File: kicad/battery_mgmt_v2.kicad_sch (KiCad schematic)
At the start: 16 parts, among them J601 BATTERY_CONN, SW401 SW_Push, U402 BQ21061

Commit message: refactor, fix issues, ready for first design
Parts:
- added TP301: VIO_TEST, symbol Connector:TestPoint
- C407: value 1uF -> 2.2uF
- TP602: value VB_TEST -> BATTP_TEST
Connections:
- net CHRG: no longer R403.1, R404.1, R405.1, R406.1
- net VIO: now reaches C404.1, U402.13 (VDD), U402.17 (VIO)
- net VIO: now also R403.1, R404.1, R405.1, R406.1, TP301.1
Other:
- note added: "Try and keep LDO connections <100-150 mA"
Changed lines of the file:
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@@
+	)
+	(junction
+		(at 170.18 83.82)
+		(diameter 0)
+		(color 0 0 0 0)
 	)
 	(junction
@@
 	)
 	(junction
-		(at 170.18 83.82)
-		(diameter 0)
-		(color 0 0 0 0)
-	)
-	(junction
 		(at 189.23 76.2)
 		(diameter 0)
@@
 		(color 0 0 0 0)
 	)
+	(junction
+		(at 170.18 86.36)
+		(diameter 0)
+		(color 0 0 0 0)
+	)
 	(wire
 		(pts
@@
 	(wire
 		(pts
+			(xy 167.64 121.92) (xy 167.64 127)
+		)
+		(stroke
+			(width 0)
+			(type default)
+		)
+	)
+	(wire
+		(pts
 			(xy 177.8 63.5) (xy 170.18 63.5)
 		)
@@
 	(wire
 		(pts
+			(xy 147.32 121.92) (xy 147.32 127)
+		)
+		(stroke
+			(width 0)
+			(type default)
+		)
+	)
+	(wire
+		(pts
 			(xy 130.81 88.9) (xy 139.7 88.9)
 		)
@@
 	(wire
 		(pts
+			(xy 176.53 121.92) (xy 176.53 127)
+		)
+		(stroke
+			(width 0)
+			(type default)
+		)
+	)
+	(wire
+		(pts
 			(xy 147.32 135.89) (xy 147.32 134.62)
 		)
@@
 	(wire
 		(pts
+			(xy 170.18 86.36) (xy 173.99 86.36)
+		)
+		(stroke
+			(width 0)
+			(type default)
+		)
+	)
+	(wire
+		(pts
 			(xy 137.16 135.89) (xy 137.16 134.62)
 		)
@@
 	(wire
 		(pts
+			(xy 97.79 133.35) (xy 97.79 137.16)
+		)
+		(stroke
+			(width 0)
+			(type default)
+		)
+	)
+	(wire
+		(pts
 			(xy 189.23 76.2) (xy 196.85 76.2)
 		)
@@
 			(width 0)
 			(type default)
+		)
+	)
+	(wire
+		(pts
+			(xy 137.16 121.92) (xy 137.16 127)
+		)
+		(stroke
+			(width 0)
+			(type default)
+		)
+	)
+	(text "Try and keep LDO\nconnections <100-150 mA"
+		(exclude_from_sim no)
+		(at 208.026 89.916 0)
+		(effects
+			(font
+				(size 1.27 1.27)
+			)
+		)
+	)
+	(label "VIO"
+		(at 97.79 133.35 270)
+		(fields_autoplaced yes)
+		(effects
+			(font
+				(size 1.27 1.27)
+			)
+			(justify right bottom)
+		)
+	)
+	(label "VIO"
+		(at 173.99 86.36 180)
+		(fields_autoplaced yes)
+		(effects
+			(font
+				(size 1.27 1.27)
+			)
+			(justify right bottom)
+		)
+	)
+	(label "VIO"
+		(at 147.32 121.92 270)
+		(fields_autoplaced yes)
+		(effects
+			(font
+				(size 1.27 1.27)
+			)
+			(justify right bottom)
+		)
+	)
+	(label "VIO"
+		(at 167.64 121.92 270)
+		(fields_autoplaced yes)
+		(effects
+			(font
+				(size 1.27 1.27)
+			)
+			(justify right bottom)
+		)
+	)
+	(label "VIO"
+		(at 176.53 121.92 270)
+		(fields_autoplaced yes)
+		(effects
+			(font
+				(size 1.27 1.27)
+			)
+			(justify right bottom)
+		)
+	)
+	(label "VIO"
+		(at 137.16 121.92 270)
+		(fields_autoplaced yes)
+		(effects
+			(font
+				(size 1.27 1.27)
+			)
+			(justify right bottom)
 		)
 	)
@@
 		)
 	)
-	(hierarchical_label "CHRG"
-		(shape input)
-		(at 167.64 127 90)
-		(fields_autoplaced yes)
-		(effects
-			(font
-				(size 1.27 1.27)
-			)
-			(justify left)
-		)
-	)
 	(hierarchical_label "PG_N"
 		(shape output)
@@
 		)
 	)
-	(hierarchical_label "CHRG"
-		(shape input)
-		(at 147.32 127 90)
-		(fields_autoplaced yes)
-		(effects
-			(font
-				(size 1.27 1.27)
-			)
-			(justify left)
-		)
-	)
 	(hierarchical_label "SCL"
 		(shape input)
@@
 		)
 	)
-	(hierarchical_label "CHRG"
-		(shape input)
-		(at 176.53 127 90)
-		(fields_autoplaced yes)
-		(effects
-			(font
-				(size 1.27 1.27)
-			)
-			(justify left)
-		)
-	)
 	(hierarchical_label "PG_N"
 		(shape output)
@@
 		)
 	)
-	(hierarchical_label "CHRG"
-		(shape input)
-		(at 137.16 127 90)
-		(fields_autoplaced yes)
-		(effects
-			(font
-				(size 1.27 1.27)
-			)
-			(justify left)
-		)
-	)
 	(hierarchical_label "SCL"
 		(shape input)
@@
 			)
 		)
-		(property "Value" "VB_TEST"
+		(property "Value" "BATTP_TEST"
 			(at 103.378 129.54 90)
 			(effects
@@
 			)
 		)
-		(property "Value" "1uF"
+		(property "Value" "2.2uF"
 			(at 199.898 82.296 0)
 			(effects
@@
 					(unit 1)
 				)
+			)
+		)
+	)
+	(symbol
+		(lib_id "Connector:TestPoint")
+		(at 97.79 137.16 270)
+		(unit 1)
+		(exclude_from_sim no)
+		(in_bom yes)
+		(on_board yes)
+		(dnp no)
+		(property "Reference" "TP301"
+			(at 89.154 138.176 90)
+			(effects
+				(font
+					(size 1.27 1.27)
+				)
+				(justify left)
+			)
+		)
+		(property "Value" "VIO_TEST"
+			(at 103.378 138.43 90)
+			(effects
+				(font
+					(size 1.27 1.27)
+				)
+				(justify left)
+			)
+		)
+		(property "Footprint" ""
+			(at 97.79 142.24 0)
+			(effects
+				(font
+					(size 1.27 1.27)
+				)
+				(hide yes)
+			)
+		)
+		(property "Datasheet" "~"
+			(at 97.79 142.24 0)
+			(effects
+				(font
+					(size 1.27 1.27)
+				)
+				(hide yes)
+			)
+		)
+		(property "Description" "test point"
+			(at 97.79 137.16 0)
+			(effects
+				(font
+					(size 1.27 1.27)
+				)
+				(hide yes)
+			)
+		)
+		(pin "1"
+		)
+		(instances
+			(project "kicad"
+				(path "/97e37379-fec6-4f0d-82d9-4ea53516bb02/d2226d13-9ee7-410c-817d-a66f223af34c"
+					(reference "TP301")
+					(unit 1)
+				)

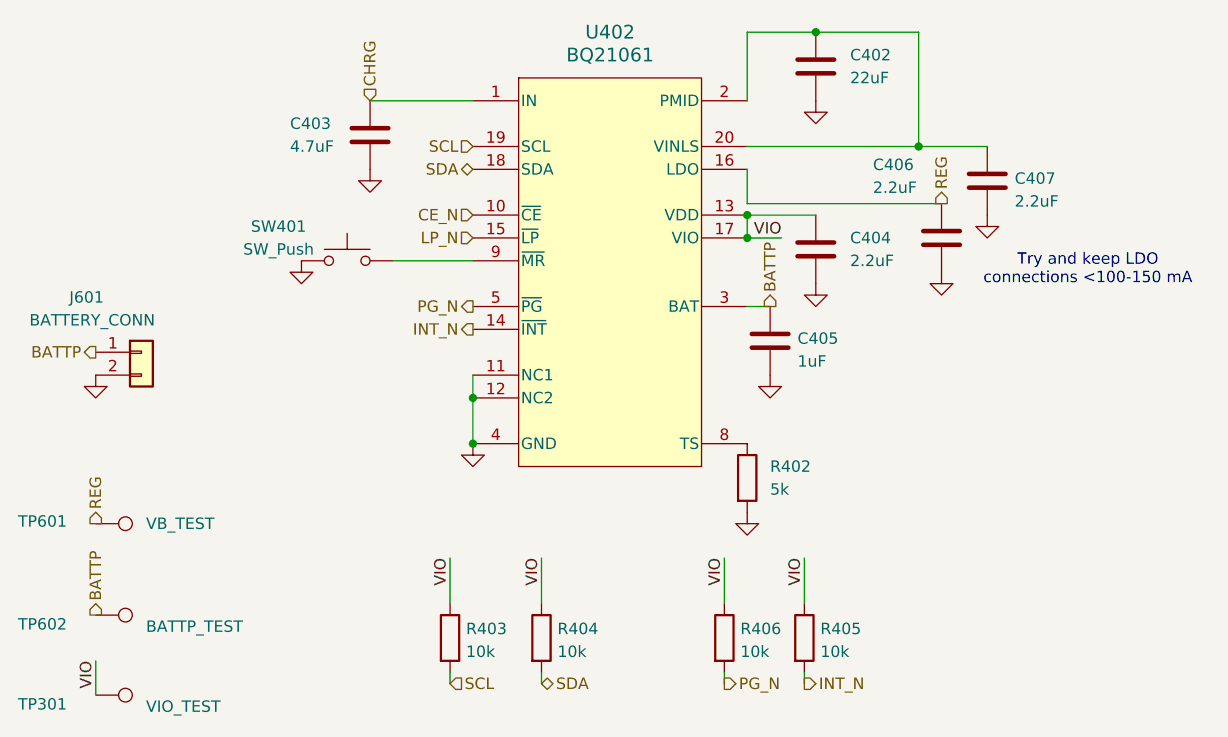
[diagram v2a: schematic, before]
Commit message: essentially finish schematic, start adding footprints, add new footprints
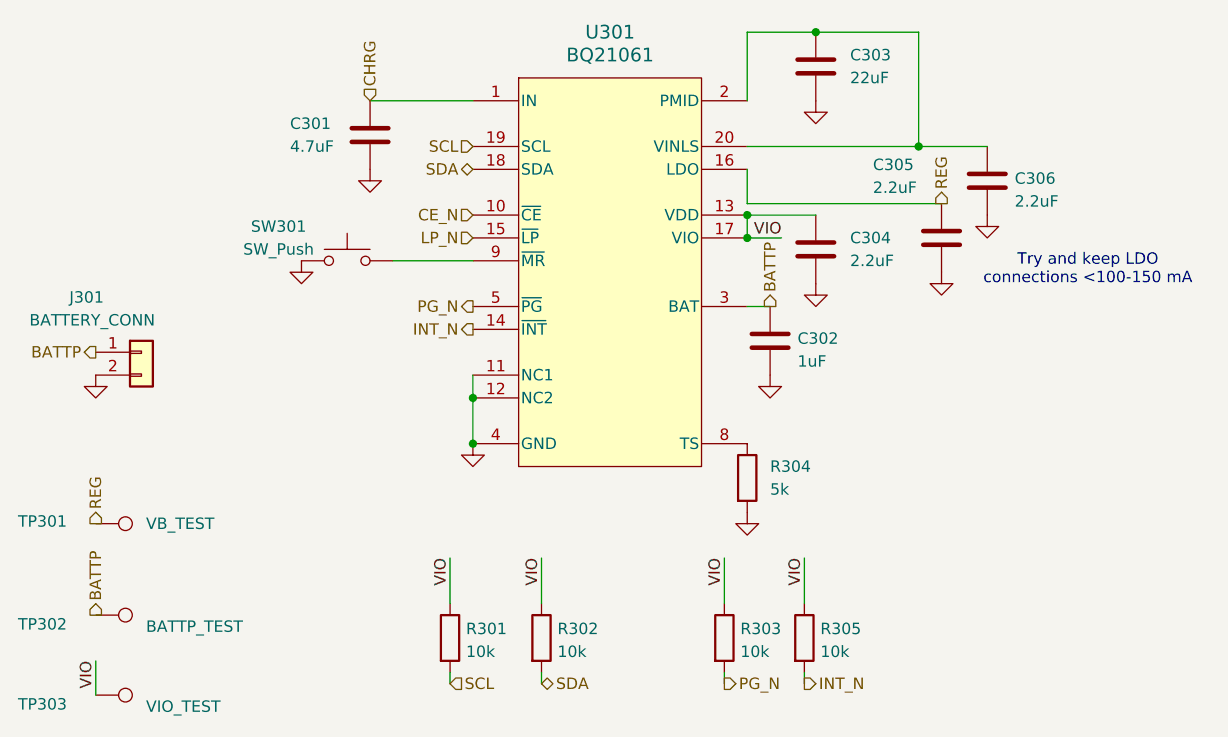
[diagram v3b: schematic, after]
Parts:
- C301: renamed from C403; footprint (none) -> Capacitor_SMD:C_0805_2012Metric_Pad1.18x1.45mm_HandSolder
- C302: renamed from C405; footprint (none) -> Capacitor_SMD:C_0805_2012Metric_Pad1.18x1.45mm_HandSolder
- C303: renamed from C402; footprint (none) -> Capacitor_SMD:C_0805_2012Metric_Pad1.18x1.45mm_HandSolder
- C304: renamed from C404; footprint (none) -> Capacitor_SMD:C_0603_1608Metric_Pad1.08x0.95mm_HandSolder
- C305: renamed from C406; footprint (none) -> Capacitor_SMD:C_0603_1608Metric_Pad1.08x0.95mm_HandSolder
- C306: renamed from C407; footprint (none) -> Capacitor_SMD:C_0603_1608Metric_Pad1.08x0.95mm_HandSolder
- J301: renamed from J601; footprint (none) -> Connector_JST:JST_PH_S2B-PH-K_1x02_P2.00mm_Horizontal
- R301: renamed from R403; footprint (none) -> Resistor_SMD:R_0603_1608Metric_Pad0.98x0.95mm_HandSolder
- R302: renamed from R404; footprint (none) -> Resistor_SMD:R_0603_1608Metric_Pad0.98x0.95mm_HandSolder
- R303: renamed from R406; footprint (none) -> Resistor_SMD:R_0603_1608Metric_Pad0.98x0.95mm_HandSolder
- R304: renamed from R402; footprint (none) -> Resistor_SMD:R_0603_1608Metric_Pad0.98x0.95mm_HandSolder
- R305: renamed from R405; footprint (none) -> Resistor_SMD:R_0603_1608Metric_Pad0.98x0.95mm_HandSolder
- SW301: renamed from SW401; footprint (none) -> Button_Switch_SMD:SW_Push_1P1T_NO_6x6mm_H9.5mm
- TP301: renamed from TP601; footprint (none) -> TestPoint:TestPoint_Pad_D3.0mm
- TP302: renamed from TP602; footprint (none) -> TestPoint:TestPoint_Pad_D3.0mm
- TP303: renamed from TP301; footprint (none) -> TestPoint:TestPoint_Pad_D3.0mm
- U301: renamed from U402; footprint YFP0020ACAC -> Raven:YFP0020ACAC

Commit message: fix motor with spring fingers, start PCB
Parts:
- TP301, TP302, TP303: footprint TestPoint:TestPoint_Pad_D3.0mm -> TestPoint:TestPoint_Pad_D1.5mm
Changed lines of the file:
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@@
 			)
 		)
-		(property "Footprint" "TestPoint:TestPoint_Pad_D3.0mm"
+		(property "Footprint" "TestPoint:TestPoint_Pad_D1.5mm"
 			(at 97.79 133.35 0)
 			(effects
@@
 			)
 		)
-		(property "Footprint" "TestPoint:TestPoint_Pad_D3.0mm"
+		(property "Footprint" "TestPoint:TestPoint_Pad_D1.5mm"
 			(at 97.79 123.19 0)
 			(effects
@@
 			)
 		)
-		(property "Footprint" "TestPoint:TestPoint_Pad_D3.0mm"
+		(property "Footprint" "TestPoint:TestPoint_Pad_D1.5mm"
 			(at 97.79 142.24 0)
 			(effects

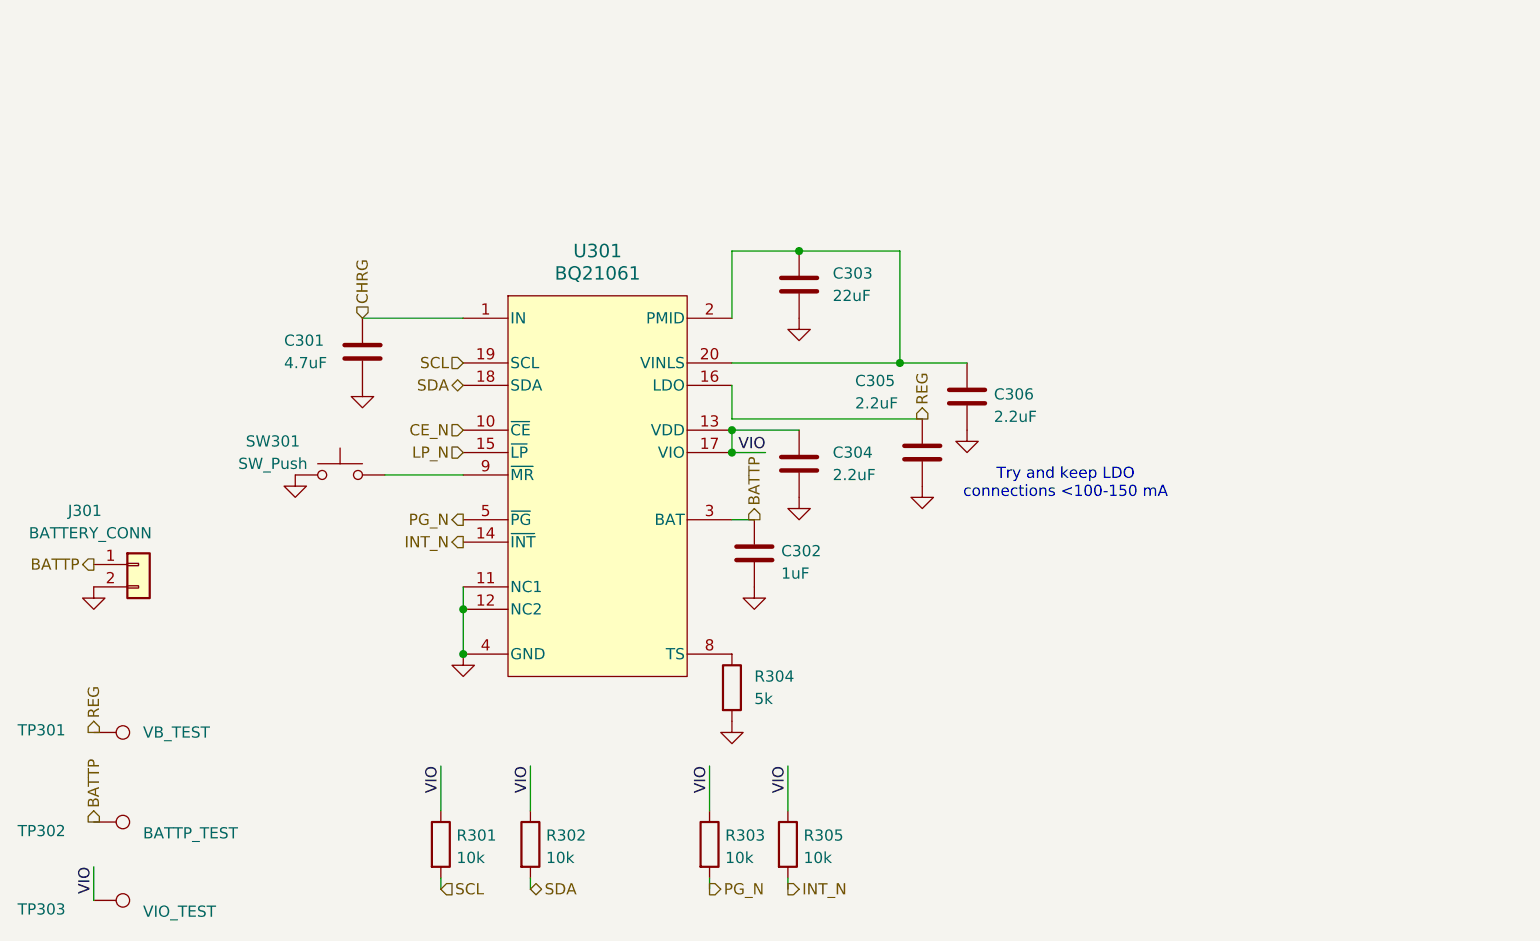
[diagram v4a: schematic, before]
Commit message: finish PCB routing, need silkscreen + checks
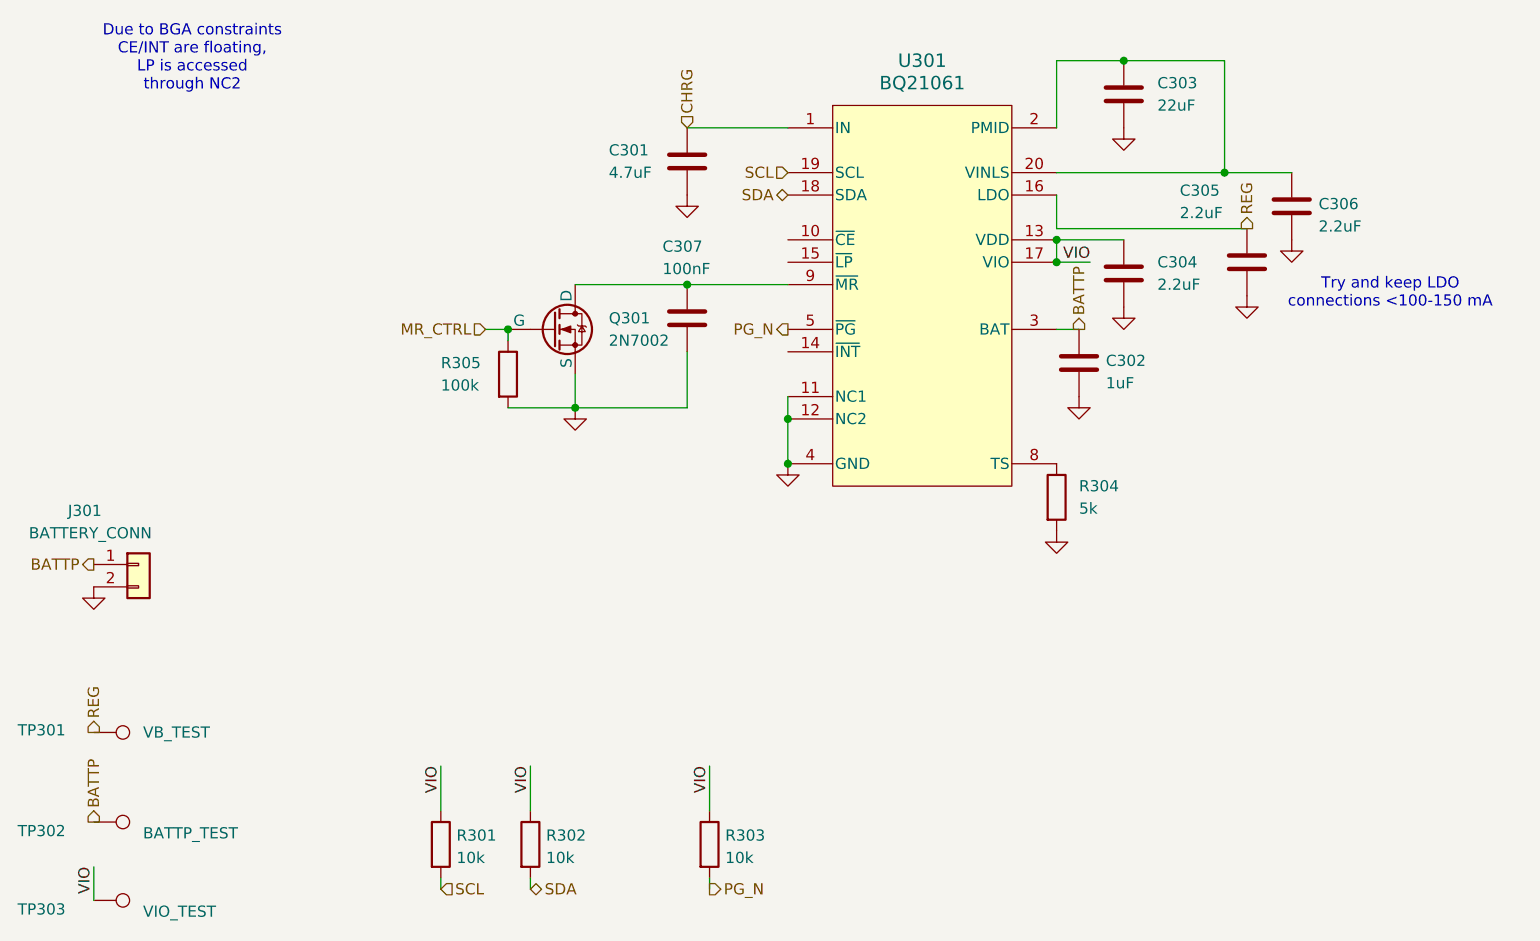
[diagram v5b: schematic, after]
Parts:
- removed SW301: SW_Push, Button_Switch_SMD:SW_Push_1P1T_NO_6x6mm_H9.5mm, symbol Switch:SW_Push
- added C307: 100nF, Capacitor_SMD:C_0603_1608Metric_Pad1.08x0.95mm_HandSolder, symbol Device:C
- added Q301: 2N7002, Package_TO_SOT_SMD:SOT-23-3, symbol Simulation_SPICE:NMOS
- R305: value 10k -> 100k
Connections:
- net GND: now also R305.2, C307.2, Q301.3 (S)
- net VIO: no longer R305.1
- net at U301.9 (~{MR}): now also C307.1, Q301.1 (D)
- net CE_N: no longer names the net of U301.10 (~{CE})
- net INT_N: no longer names the net of U301.14 (~{INT})
- net INT_N: no longer R305.2
- net LP_N: no longer names the net of U301.15 (~{LP})
- new net MR_CTRL: Q301.2 (G), R305.1
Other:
- note added: "Due to BGA constraints CE/INT are floating, LP is accessed through NC2"
- moved on the sheet: C301, C302, C303, C304, C305, C306, R304, U301

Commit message: add some assembly files, but transition towards all hand
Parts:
- C301, J301, Q301, R304, TP301, TP302, TP303: JLC (none) -> XXXXXX; LCSC (none) -> XXXXXX
- C302, C303: JLC (none) -> 0805
- C304, C305, C306, C307, R301, R302, R303, R305: JLC (none) -> 0603
- U301: footprint Raven:YFP0020ACAC -> Raven:WSON10_DLH_TEX-M; JLC (none) -> DSBGA-20; LCSC (none) -> C2869893
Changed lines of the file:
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@@
+			)
+		)
+		(property "JLC" "XXXXXX"
+			(at 102.87 99.06 0)
+			(effects
+				(font
+					(size 1.27 1.27)
+				)
+				(hide yes)
+			)
+		)
+		(property "LCSC" "XXXXXX"
+			(at 102.87 99.06 0)
+			(effects
+				(font
+					(size 1.27 1.27)
+				)
+				(hide yes)
 			)
 		)
@@
 			)
 		)
+		(property "JLC" "0603"
+			(at 144.78 77.47 0)
+			(effects
+				(font
+					(size 1.27 1.27)
+				)
+				(hide yes)
+			)
+		)
 		(pin "2"
 		)
@@
 			)
 		)
+		(property "JLC" "XXXXXX"
+			(at 97.79 128.27 0)
+			(effects
+				(font
+					(size 1.27 1.27)
+				)
+				(hide yes)
+			)
+		)
+		(property "LCSC" "XXXXXX"
+			(at 97.79 128.27 0)
+			(effects
+				(font
+					(size 1.27 1.27)
+				)
+				(hide yes)
+			)
+		)
 		(pin "1"
 		)
@@
 		)
 		(property "Description" "Unpolarized capacitor"
+			(at 228.6 64.77 0)
+			(effects
+				(font
+					(size 1.27 1.27)
+				)
+				(hide yes)
+			)
+		)
+		(property "JLC" "0603"
 			(at 228.6 64.77 0)
 			(effects
@@
 			)
 		)
-		(property "Footprint" "Raven:YFP0020ACAC"
+		(property "Footprint" "Raven:WSON10_DLH_TEX-M"
 			(at 191.77 67.31 0)
 			(effects
@@
 		)
 		(property "Description" ""
+			(at 191.77 67.31 0)
+			(effects
+				(font
+					(size 1.27 1.27)
+				)
+				(hide yes)
+			)
+		)
+		(property "JLC" "DSBGA-20"
+			(at 191.77 67.31 0)
+			(effects
+				(font
+					(size 1.27 1.27)
+				)
+				(hide yes)
+			)
+		)
+		(property "LCSC" "C2869893"
 			(at 191.77 67.31 0)
 			(effects
@@
 			)
 		)
+		(property "JLC" "XXXXXX"
+			(at 97.79 118.11 0)
+			(effects
+				(font
+					(size 1.27 1.27)
+				)
+				(hide yes)
+			)
+		)
+		(property "LCSC" "XXXXXX"
+			(at 97.79 118.11 0)
+			(effects
+				(font
+					(size 1.27 1.27)
+				)
+				(hide yes)
+			)
+		)
 		(pin "1"
 		)
@@
 			)
 		)
+		(property "JLC" "0603"
+			(at 214.63 66.04 0)
+			(effects
+				(font
+					(size 1.27 1.27)
+				)
+				(hide yes)
+			)
+		)
 		(pin "2"
 		)
@@
 			)
 		)
+		(property "JLC" "XXXXXX"
+			(at 207.01 91.44 0)
+			(effects
+				(font
+					(size 1.27 1.27)
+				)
+				(hide yes)
+			)
+		)
+		(property "LCSC" "XXXXXX"
+			(at 207.01 91.44 0)
+			(effects
+				(font
+					(size 1.27 1.27)
+				)
+				(hide yes)
+			)
+		)
 		(pin "1"
 		)
@@
 			)
 		)
+		(property "JLC" "0603"
+			(at 137.16 130.81 0)
+			(effects
+				(font
+					(size 1.27 1.27)
+				)
+				(hide yes)
+			)
+		)
 		(pin "1"
 		)
@@
 			)
 		)
+		(property "JLC" "0603"
+			(at 165.1 71.12 0)
+			(effects
+				(font
+					(size 1.27 1.27)
+				)
+				(hide yes)
+			)
+		)
 		(pin "2"
 		)
@@
 			)
 		)
+		(property "JLC" "XXXXXX"
+			(at 149.86 72.39 0)
+			(effects
+				(font
+					(size 1.27 1.27)
+				)
+				(hide yes)
+			)
+		)
+		(property "LCSC" "XXXXXX"
+			(at 149.86 72.39 0)
+			(effects
+				(font
+					(size 1.27 1.27)
+				)
+				(hide yes)
+			)
+		)
 		(pin "3"
 		)
@@
 			)
 		)
+		(property "JLC" "0603"
+			(at 167.64 130.81 0)
+			(effects
+				(font
+					(size 1.27 1.27)
+				)
+				(hide yes)
+			)
+		)
 		(pin "1"
 		)
@@
 			)
 		)
+		(property "JLC" "XXXXXX"
+			(at 165.1 53.34 0)
+			(effects
+				(font
+					(size 1.27 1.27)
+				)
+				(hide yes)
+			)
+		)
+		(property "LCSC" "XXXXXX"
+			(at 165.1 53.34 0)
+			(effects
+				(font
+					(size 1.27 1.27)
+				)
+				(hide yes)
+			)
+		)
 		(pin "2"
 		)
@@
 			)
 		)
+		(property "JLC" "0805"
+			(at 209.55 76.2 0)
+			(effects
+				(font
+					(size 1.27 1.27)
+				)
+				(hide yes)
+			)
+		)
 		(pin "2"
 		)
@@
 			)
 		)
+		(property "JLC" "0603"
+			(at 233.68 58.42 0)
+			(effects
+				(font
+					(size 1.27 1.27)
+				)
+				(hide yes)
+			)
+		)
 		(pin "2"
 		)
@@
 		)
 		(property "Description" "test point"
+			(at 97.79 137.16 0)
+			(effects
+				(font
+					(size 1.27 1.27)
+				)
+				(hide yes)
+			)
+		)
+		(property "JLC" "XXXXXX"
+			(at 97.79 137.16 0)
+			(effects
+				(font
+					(size 1.27 1.27)
+				)
+				(hide yes)
+			)
+		)
+		(property "LCSC" "XXXXXX"
 			(at 97.79 137.16 0)
 			(effects
@@
 			)
 		)
+		(property "JLC" "0805"
+			(at 214.63 45.72 0)
+			(effects
+				(font
+					(size 1.27 1.27)
+				)
+				(hide yes)
+			)
+		)
 		(pin "2"
 		)
@@
 			(at 147.32 130.81 0)
 			(effects
+				(font
+					(size 1.27 1.27)
+				)
+				(hide yes)
+			)
+		)
+		(property "JLC" "0603"
+			(at 147.32 130.81 0)
+			(effects
